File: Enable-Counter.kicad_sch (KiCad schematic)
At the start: 9 parts, among them SW1 SW_Push, U3 SN74LVC112AD, U4 74LVC1G04, U5 74LVC1G04, U6 TLC555xD

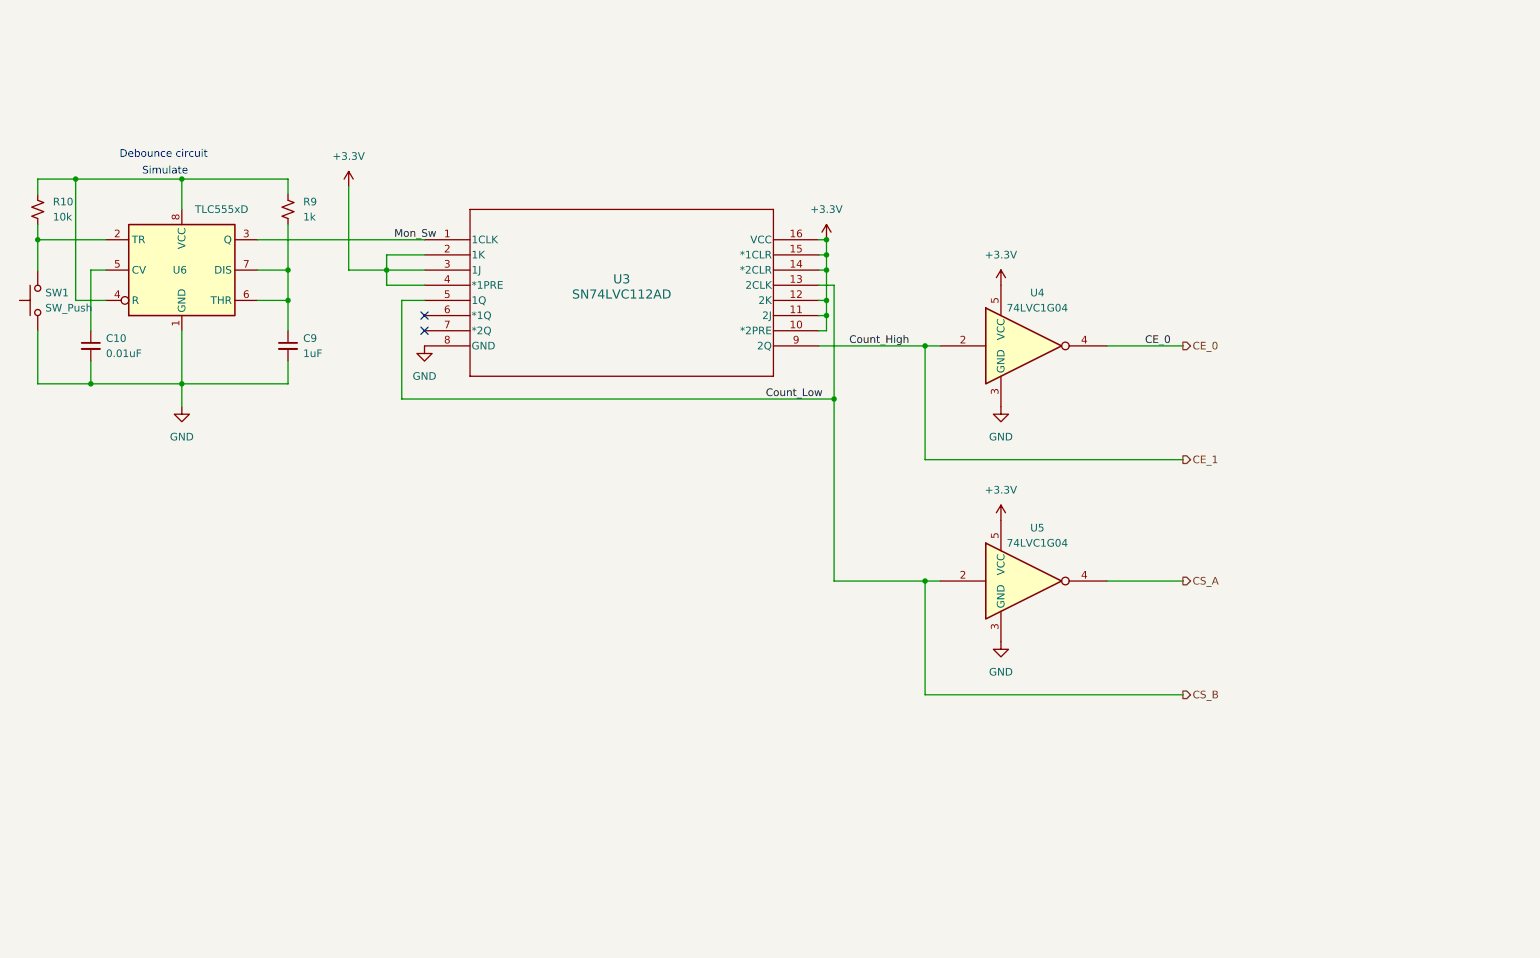
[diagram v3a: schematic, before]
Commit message: Add LED indicator logic
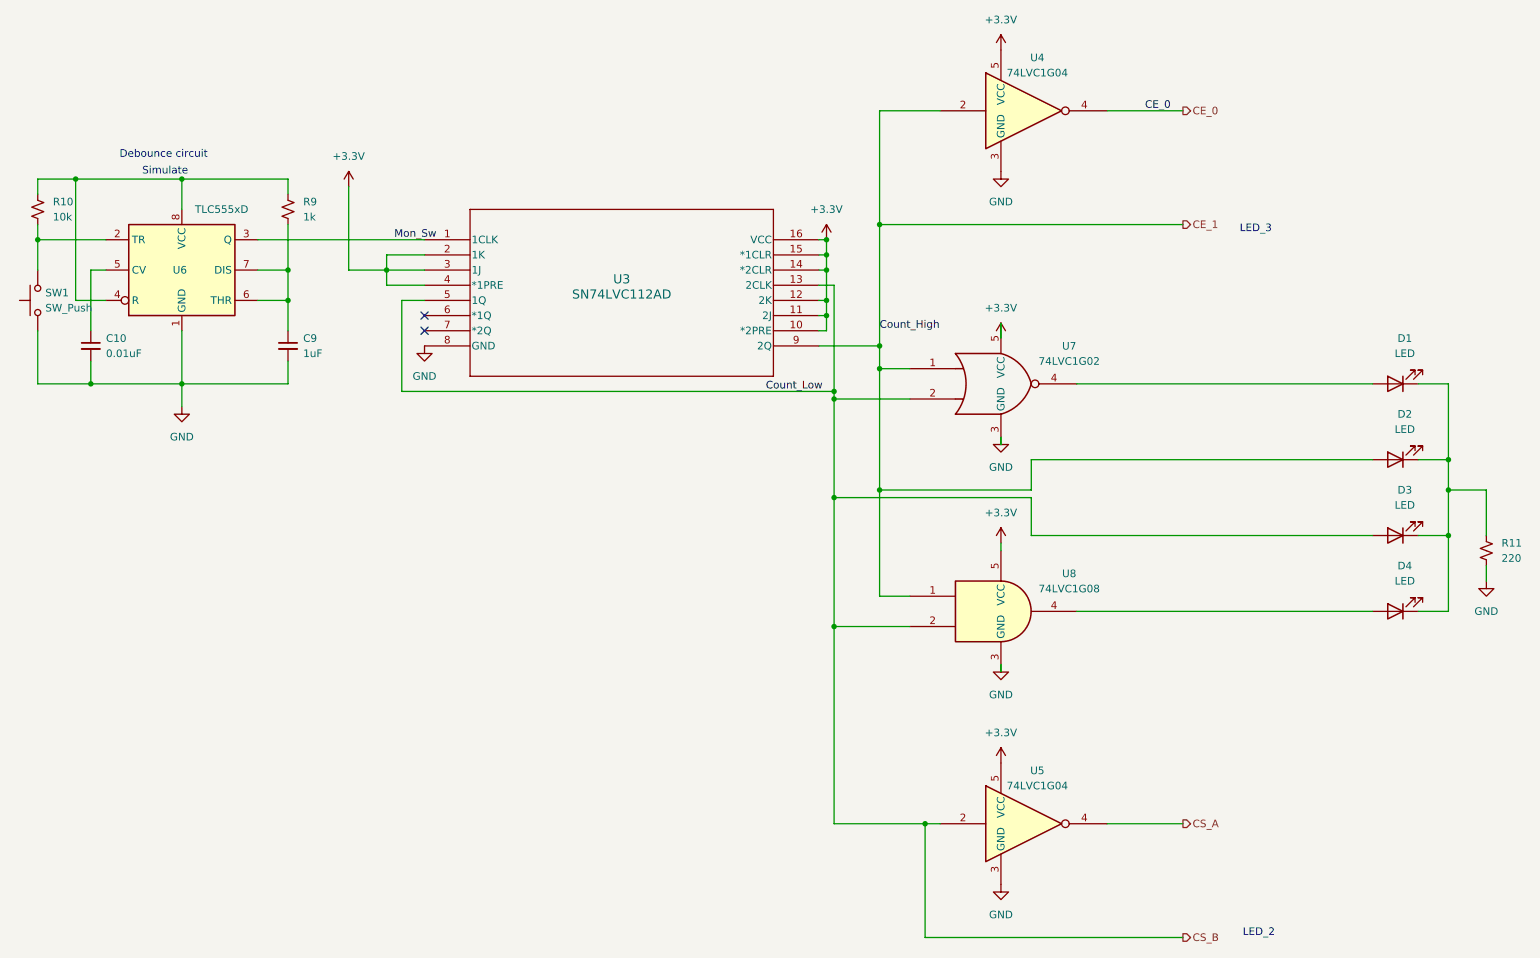
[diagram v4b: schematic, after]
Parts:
- added D1, D2, D3, D4: LED, symbol Device:LED
- added R11: 220, symbol Device:R_Small_US
- added U7: 74LVC1G02, symbol 74xGxx:74LVC1G02
- added U8: 74LVC1G08, symbol 74xGxx:74LVC1G08
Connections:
- net +3.3V: now also U7.5 (VCC), U8.5 (VCC)
- net CE_1: now also D2.2 (A), U7.1, U8.1
- net CS_B: now also D3.2 (A), U7.2, U8.2
- net GND: now also R11.2, U7.3 (GND), U8.3 (GND)
- new net: D1.1 (K), D2.1 (K), D3.1 (K), D4.1 (K), R11.1
- new net: D1.2 (A), U7.4
- new net: D4.2 (A), U8.4
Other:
- note added: "LED_2"
- note added: "LED_3"
- moved on the sheet: U4, U5

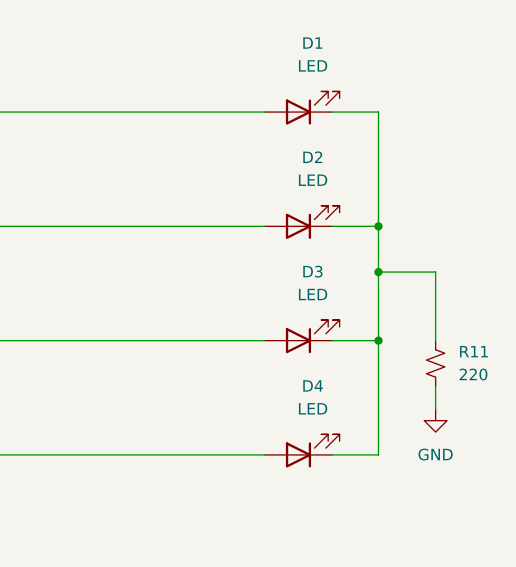
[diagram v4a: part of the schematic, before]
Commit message: Begin USB switching
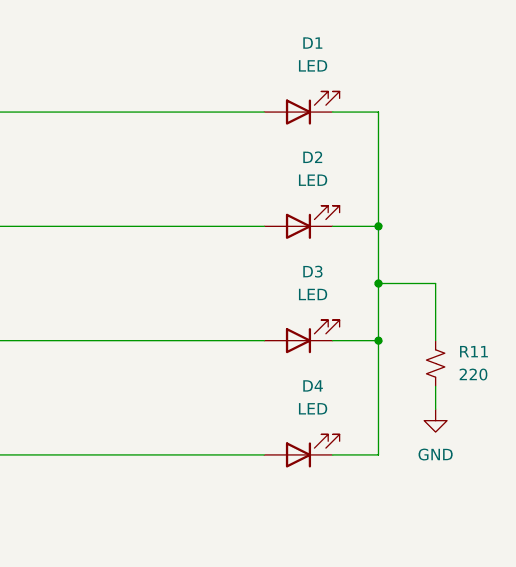
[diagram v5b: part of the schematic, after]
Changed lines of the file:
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@@
 	(paper "USLetter")
 	(junction
+		(at 254 95.25)
+		(diameter 0)
+		(color 0 0 0 0)
+	)
+	(junction
 		(at 158.75 69.85)
 		(diameter 0)
@@
 	(junction
 		(at 254 88.9)
-		(diameter 0)
-		(color 0 0 0 0)
-	)
-	(junction
-		(at 254 93.98)
 		(diameter 0)
 		(color 0 0 0 0)
@@
 	(wire
 		(pts
-			(xy 254 88.9) (xy 254 93.98)
-		)
-		(stroke
-			(width 0)
-			(type default)
-		)
-	)
-	(wire
-		(pts
 			(xy 158.75 49.53) (xy 158.75 69.85)
 		)
@@
 	(wire
 		(pts
-			(xy 254 93.98) (xy 260.35 93.98)
+			(xy 254 95.25) (xy 260.35 95.25)
 		)
 		(stroke
@@
 	(wire
 		(pts
+			(xy 254 95.25) (xy 254 101.6)
+		)
+		(stroke
+			(width 0)
+			(type default)
+		)
+	)
+	(wire
+		(pts
 			(xy 158.75 73.66) (xy 163.83 73.66)
 		)
@@
 	(wire
 		(pts
-			(xy 254 93.98) (xy 254 101.6)
+			(xy 254 88.9) (xy 254 95.25)
 		)
 		(stroke
@@
 	(wire
 		(pts
-			(xy 260.35 93.98) (xy 260.35 101.6)
-		)
-		(stroke
+			(xy 260.35 95.25) (xy 260.35 101.6)
+		)
+		(stroke
